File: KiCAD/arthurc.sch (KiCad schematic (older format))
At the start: 52 parts, among them IC1 ATMEGA328, P1 I/O, P10 CD2, P11 CD2, P12 CD1, P13 CD1, P4 CONN_6, P5 CONN_6, P6 9VBAT, P7 GPS, P8 FTDI, P9 ISP, SW1 SW_PUSH, U1 3V3, U2 74HC125, U3 5V0, X1 16MHz

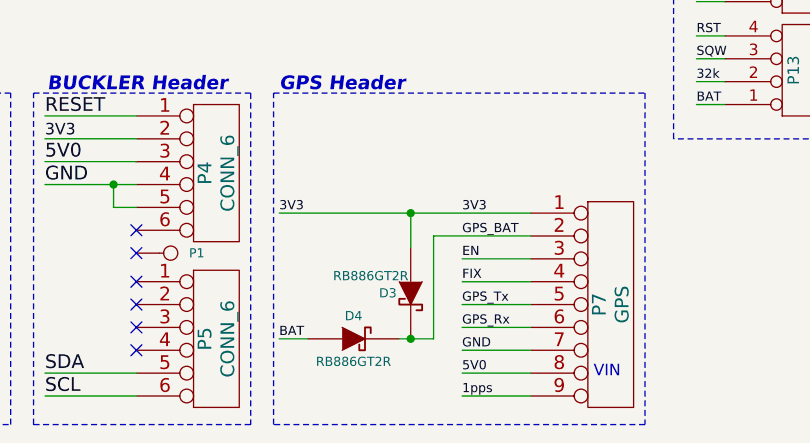
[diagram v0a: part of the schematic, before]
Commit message: Ultimate GPS header added to I2GPS
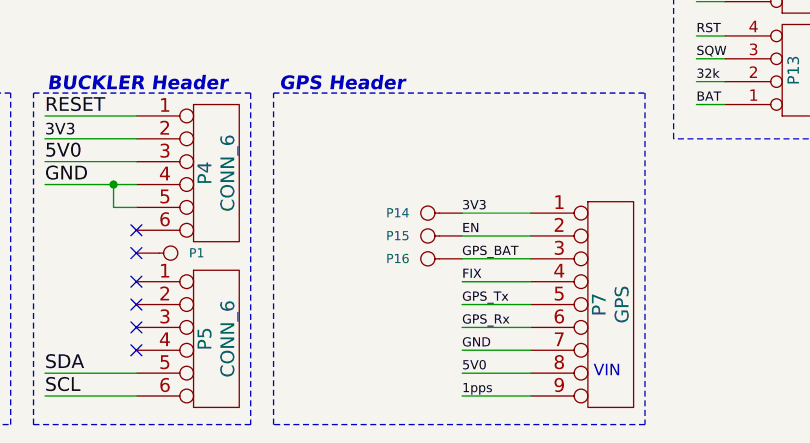
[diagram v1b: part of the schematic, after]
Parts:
- removed D3, D4: RB886GT2R, d_VMD2, symbol DIODESCH
- added P14, P15, P16: I/O, ArthurC Lib:I%2fO, symbol I/O
- B10, B11, B16, B17: footprint I/O_ADR -> ArthurC Lib:I%2fO_ADR
- B18, B19, B4, B5, B6, B8, P1: footprint I/O -> ArthurC Lib:I%2fO
- P7: footprint (none) -> ArthurC Lib:PIN_ARRAY-9X1
- X1: footprint (none) -> ArthurC Lib:Xtal_SMD3
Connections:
- wire segments 227 -> 223
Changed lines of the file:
@@
 MCP1700T-3302E/TT
-Wire Wire Line
-	5375 7375 5250 7375
 Wire Wire Line
 	3400 2750 4800 2750
@@
 Wire Wire Line
 	2450 4850 2450 5100
-Wire Wire Line
-	5775 7375 5925 7375
-Connection ~ 5825 7375
-$Comp
-L DIODESCH D4
-U 1 1 4F9A5A10
-P 5575 7375
-F 0 "D4" H 5575 7475 40  0000 C CNN
-F 1 "RB886GT2R" H 5575 7275 40  0000 C CNN
-F 2 "d_VMD2" H 5575 7375 40  0001 C CNN
-F 3 "" H 5575 7375 60  0001 C CNN
-	1    5575 7375
-	1    0    0    -1
-$EndComp
-$Comp
-L DIODESCH D3
-U 1 1 4F9A5A02
-P 5825 7175
-F 0 "D3" V 5825 7075 40  0000 C CNN
-F 1 "RB886GT2R" V 5750 7000 40  0000 C CNN
-F 2 "d_VMD2" V 5850 7000 40  0001 C CNN
-F 3 "" H 5825 7175 60  0001 C CNN
-	1    5825 7175
-	0    1    1    0
-$EndComp
 Text Label 1400 3275 0    50   ~ 0
 PB7
@@
 PB6
 $Comp
-L GND #PWR01
+L GND #PWR1
 U 1 1 4F5AFC62
 P 2450 5100
-F 0 "#PWR01" H 2450 5100 30  0001 C CNN
+F 0 "#PWR1" H 2450 5100 30  0001 C CNN
 F 1 "GND" H 2450 5030 30  0001 C CNN
 F 2 "" H 2450 5100 60  0001 C CNN
@@
 Text Notes 5250 6300 0    60   Italic 12
 GPS Header
-Text Label 5250 7375 0    40   ~ 0
-BAT
-Text Label 5250 6825 0    40   ~ 0
-3V3
 Text Label 10050 1450 0    50   ~ 0
 GND
@@
 IR SENSOR
 $Comp
-L GND #PWR02
+L GND #PWR3
 U 1 1 4EC6563E
 P 4100 2250
-F 0 "#PWR02" H 4100 2250 30  0001 C CNN
+F 0 "#PWR3" H 4100 2250 30  0001 C CNN
 F 1 "GND" H 4100 2180 30  0001 C CNN
 F 2 "" H 4100 2250 60  0001 C CNN
@@
 F 0 "B19" H 4280 1950 40  0000 L CNN
 F 1 "I/O" H 4200 2005 30  0001 C CNN
-F 2 "I/O" H 4200 1950 60  0001 C CNN
+F 2 "ArthurC Lib:I%2fO" H 4200 1950 60  0001 C CNN
 F 3 "" H 4200 1950 60  0001 C CNN
 	1    4200 1950
@@
 F 0 "B18" H 4180 1950 40  0000 L CNN
 F 1 "I/O" H 4100 2005 30  0001 C CNN
-F 2 "I/O" H 4100 1950 60  0001 C CNN
+F 2 "ArthurC Lib:I%2fO" H 4100 1950 60  0001 C CNN
 F 3 "" H 4100 1950 60  0001 C CNN
 	1    4100 1950
@@
 GND
 $Comp
-L GND #PWR03
+L GND #PWR4
 U 1 1 4E96D558
 P 4500 4600
-F 0 "#PWR03" H 4500 4600 30  0001 C CNN
+F 0 "#PWR4" H 4500 4600 30  0001 C CNN
 F 1 "GND" H 4500 4530 30  0001 C CNN
 F 2 "" H 4500 4600 60  0001 C CNN
@@
 F 0 "B17" H 4305 4150 40  0000 L CNN
 F 1 "I/O" H 4225 4205 30  0001 C CNN
-F 2 "I/O_ADR" H 4225 4150 60  0001 C CNN
+F 2 "ArthurC Lib:I%2fO_ADR" H 4225 4150 60  0001 C CNN
 F 3 "" H 4225 4150 60  0001 C CNN
 	1    4225 4150
@@
 F 0 "B16" H 4305 4050 40  0000 L CNN
 F 1 "I/O" H 4225 4105 30  0001 C CNN
-F 2 "I/O_ADR" H 4225 4050 60  0001 C CNN
+F 2 "ArthurC Lib:I%2fO_ADR" H 4225 4050 60  0001 C CNN
 F 3 "" H 4225 4050 60  0001 C CNN
 	1    4225 4050
@@
 F 0 "P1" H 4855 7000 40  0000 L CNN
 F 1 "I/O" H 4775 7055 30  0001 C CNN
-F 2 "I/O" H 4775 7000 60  0001 C CNN
+F 2 "ArthurC Lib:I%2fO" H 4775 7000 60  0001 C CNN
 F 3 "" H 4775 7000 60  0001 C CNN
 	1    4775 7000
@@
 GND
 $Comp
-L +3.3V #PWR04
+L +3.3V #PWR5
 U 1 1 4E1EF3E1
 P 7600 975
-F 0 "#PWR04" H 7600 935 30  0001 C CNN
+F 0 "#PWR5" H 7600 935 30  0001 C CNN
 F 1 "+3.3V" H 7600 1085 30  0000 C CNN
 F 2 "" H 7600 975 60  0001 C CNN
@@
 $EndComp
 $Comp
-L GND #PWR05
+L GND #PWR6
 U 1 1 4E1EC9C3
 P 9950 1525
-F 0 "#PWR05" H 9950 1525 30  0001 C CNN
+F 0 "#PWR6" H 9950 1525 30  0001 C CNN
 F 1 "GND" H 9950 1455 30  0001 C CNN
 F 2 "" H 9950 1525 60  0001 C CNN
@@
 LED2
 $Comp
-L GND #PWR06
+L GND #PWR2
 U 1 1 4DCFFB44
 P 3625 7550
-F 0 "#PWR06" H 3625 7550 30  0001 C CNN
+F 0 "#PWR2" H 3625 7550 30  0001 C CNN
 F 1 "GND" H 3625 7480 30  0001 C CNN
 F 2 "" H 3625 7550 60  0001 C CNN
@@
 F 0 "B11" H 3855 4050 40  0000 L CNN
 F 1 "I/O" H 3775 4105 30  0001 C CNN
-F 2 "I/O_ADR" H 3775 4050 60  0001 C CNN
+F 2 "ArthurC Lib:I%2fO_ADR" H 3775 4050 60  0001 C CNN
 F 3 "" H 3775 4050 60  0001 C CNN
 	1    3775 4050
@@
 F 0 "B10" H 3855 4150 40  0000 L CNN
 F 1 "I/O" H 3775 4205 30  0001 C CNN
-F 2 "I/O_ADR" H 3775 4150 60  0001 C CNN
+F 2 "ArthurC Lib:I%2fO_ADR" H 3775 4150 60  0001 C CNN
 F 3 "" H 3775 4150 60  0001 C CNN
 	1    3775 4150
@@
 F 0 "B8" H 3855 2950 40  0000 L CNN
 F 1 "I/O" H 3775 3005 30  0001 C CNN
-F 2 "I/O" H 3775 2950 60  0001 C CNN
+F 2 "ArthurC Lib:I%2fO" H 3775 2950 60  0001 C CNN
 F 3 "" H 3775 2950 60  0001 C CNN
 	1    3775 2950
@@
 F 0 "B6" H 3855 2350 40  0000 L CNN
 F 1 "I/O" H 3775 2405 30  0001 C CNN
-F 2 "I/O" H 3775 2350 60  0001 C CNN
+F 2 "ArthurC Lib:I%2fO" H 3775 2350 60  0001 C CNN
 F 3 "" H 3775 2350 60  0001 C CNN
 	1    3775 2350
@@
 F 0 "B5" H 3855 2450 40  0000 L CNN
 F 1 "I/O" H 3775 2505 30  0001 C CNN
-F 2 "I/O" H 3775 2450 60  0001 C CNN
+F 2 "ArthurC Lib:I%2fO" H 3775 2450 60  0001 C CNN
 F 3 "" H 3775 2450 60  0001 C CNN
 	1    3775 2450
@@
 F 0 "B4" H 4080 1950 40  0000 L CNN
 F 1 "I/O" H 4000 2005 30  0001 C CNN
-F 2 "I/O" H 4000 1950 60  0001 C CNN
+F 2 "ArthurC Lib:I%2fO" H 4000 1950 60  0001 C CNN
 F 3 "" H 4000 1950 60  0001 C CNN
 	1    4000 1950
@@
 GND
 $Comp
-L GND #PWR07
+L GND #PWR7
 U 1 1 4DCAC327
 P 9950 2475
-F 0 "#PWR07" H 9950 2475 30  0001 C CNN
+F 0 "#PWR7" H 9950 2475 30  0001 C CNN
 F 1 "GND" H 9950 2405 30  0001 C CNN
 F 2 "" H 9950 2475 60  0001 C CNN
@@
 F 0 "P7" V 6650 7225 60  0000 C CNN
 F 1 "GPS" V 6750 7225 60  0000 C CNN
-F 2 "" H 6700 7375 60  0000 C CNN
+F 2 "ArthurC Lib:PIN_ARRAY-9X1" H 6700 7375 60  0001 C CNN
 F 3 "" H 6700 7375 60  0000 C CNN
 	1    6700 7225
@@
 	6050 7125 6350 7125
 Wire Wire Line
-	5250 6825 6350 6825
-Wire Wire Line
-	5925 6925 6350 6925
-Wire Wire Line
 	6050 7025 6350 7025
+Text Label 6050 7025 0    40   ~ 0
+GPS_BAT
 Text Label 6050 6925 0    40   ~ 0
-GPS_BAT
-Text Label 6050 7025 0    40   ~ 0
 EN
 Text Label 6050 7125 0    40   ~ 0
@@
 Text Label 6050 7625 0    40   ~ 0
 1pps
-Wire Wire Line
-	5825 6975 5825 6825
-Wire Wire Line
-	5925 7375 5925 6925
-Connection ~ 5825 6825
 Text Label 6050 6825 0    40   ~ 0
 3V3
@@
 VIN
 $Comp
-L PWR_FLAG #FLG08
+L PWR_FLAG #FLG2
 U 1 1 53135BD8
 P 2450 750
-F 0 "#FLG08" H 2450 1020 30  0001 C CNN
+F 0 "#FLG2" H 2450 1020 30  0001 C CNN
 F 1 "PWR_FLAG" H 2450 980 30  0000 C CNN
 F 2 "" H 2450 750 60  0000 C CNN
@@
 $EndComp
 $Comp
-L PWR_FLAG #FLG09
+L PWR_FLAG #FLG1
 U 1 1 53135E05
 P 2350 5100
-F 0 "#FLG09" H 2350 5370 30  0001 C CNN
+F 0 "#FLG1" H 2350 5370 30  0001 C CNN
 F 1 "PWR_FLAG" H 2350 5330 30  0000 C CNN
 F 2 "" H 2350 5100 60  0000 C CNN
@@
 F 0 "X1" V 975 3300 60  0000 C CNN
 F 1 "16MHz" V 875 3375 60  0000 C CNN
-F 2 "" H 900 3050 60  0000 C CNN
+F 2 "ArthurC Lib:Xtal_SMD3" H 900 3050 60  0001 C CNN
 F 3 "" H 900 3050 60  0000 C CNN
 	1    900  3050
 	0    1    1    0
 $EndComp
+Wire Wire Line
+	6350 6825 6050 6825
+$Comp
+L I/O P14
+U 1 1 5339A614
+P 5900 6825
+F 0 "P14" H 5980 6825 40  0000 L CNN
+F 1 "I/O" H 5900 6880 30  0001 C CNN
+F 2 "ArthurC Lib:I%2fO" H 5900 6825 60  0001 C CNN
+F 3 "" H 5900 6825 60  0001 C CNN
+	1    5900 6825
+	-1   0    0    1
+$EndComp
+Wire Wire Line
+	6350 6925 6050 6925
+$Comp
+L I/O P15
+U 1 1 5339B720
+P 5900 6925
+F 0 "P15" H 5980 6925 40  0000 L CNN
+F 1 "I/O" H 5900 6980 30  0001 C CNN
+F 2 "ArthurC Lib:I%2fO" H 5900 6925 60  0001 C CNN
+F 3 "" H 5900 6925 60  0001 C CNN
+	1    5900 6925
+	-1   0    0    1
+$EndComp
+$Comp
+L I/O P16
+U 1 1 5339B72B
+P 5900 7025
+F 0 "P16" H 5980 7025 40  0000 L CNN
+F 1 "I/O" H 5900 7080 30  0001 C CNN
+F 2 "ArthurC Lib:I%2fO" H 5900 7025 60  0001 C CNN
+F 3 "" H 5900 7025 60  0001 C CNN
+	1    5900 7025
+	-1   0    0    1
+$EndComp
 $EndSCHEMATC

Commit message: work in progress, converting design to work on 3V3
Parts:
- removed C3: 2u2 Tant, c_0805, symbol C_POL
- removed C4, C8: 100n, c_0805, symbol C
- removed C6: 47u,10V, C_ELCO_SMD, symbol C_POL
- removed R3, R4, R6: 10k, r_0805, symbol R
- removed SD1: SD_CARD_MICRO, SD_Micro, symbol SD_CARD_MICRO
- removed U2: 74HC125, SO14E, symbol 74LS125
- removed U3: 5V0, SOT23-5, symbol MIC5219-5.0
- added P2: AREF, symbol CONN_2
- added SD1: SD_CARD_Micro, symbol SD_CARD_Micro
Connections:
- net labels removed: 5V0
- wire segments 223 -> 168
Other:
- note removed: "MIC5219-5.0BM5"

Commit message: ArthurC work in progress
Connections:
- net 3Vgps: now reaches P14.1, P7.1
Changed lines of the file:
@@
 Connection ~ 5000 800
 NoConn ~ 4625 6600
+Text Label 6075 6825 0    40   ~ 0
+3Vgps
 $EndSCHEMATC

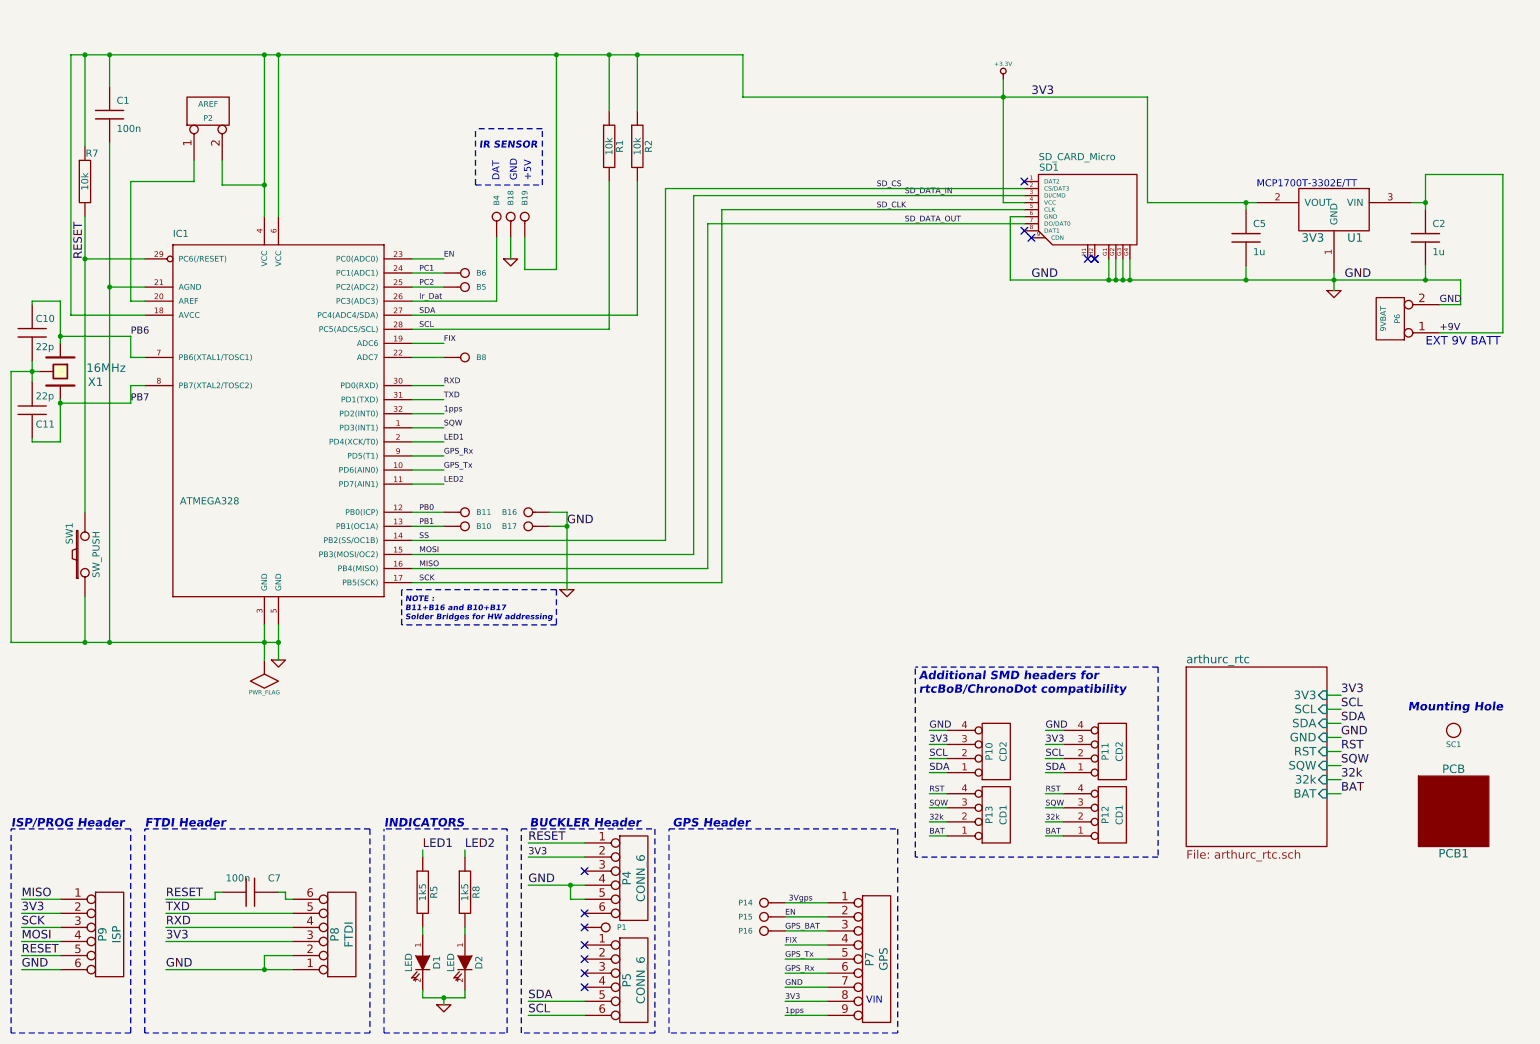
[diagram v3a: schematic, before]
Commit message: schematic needs final review before starting board layout
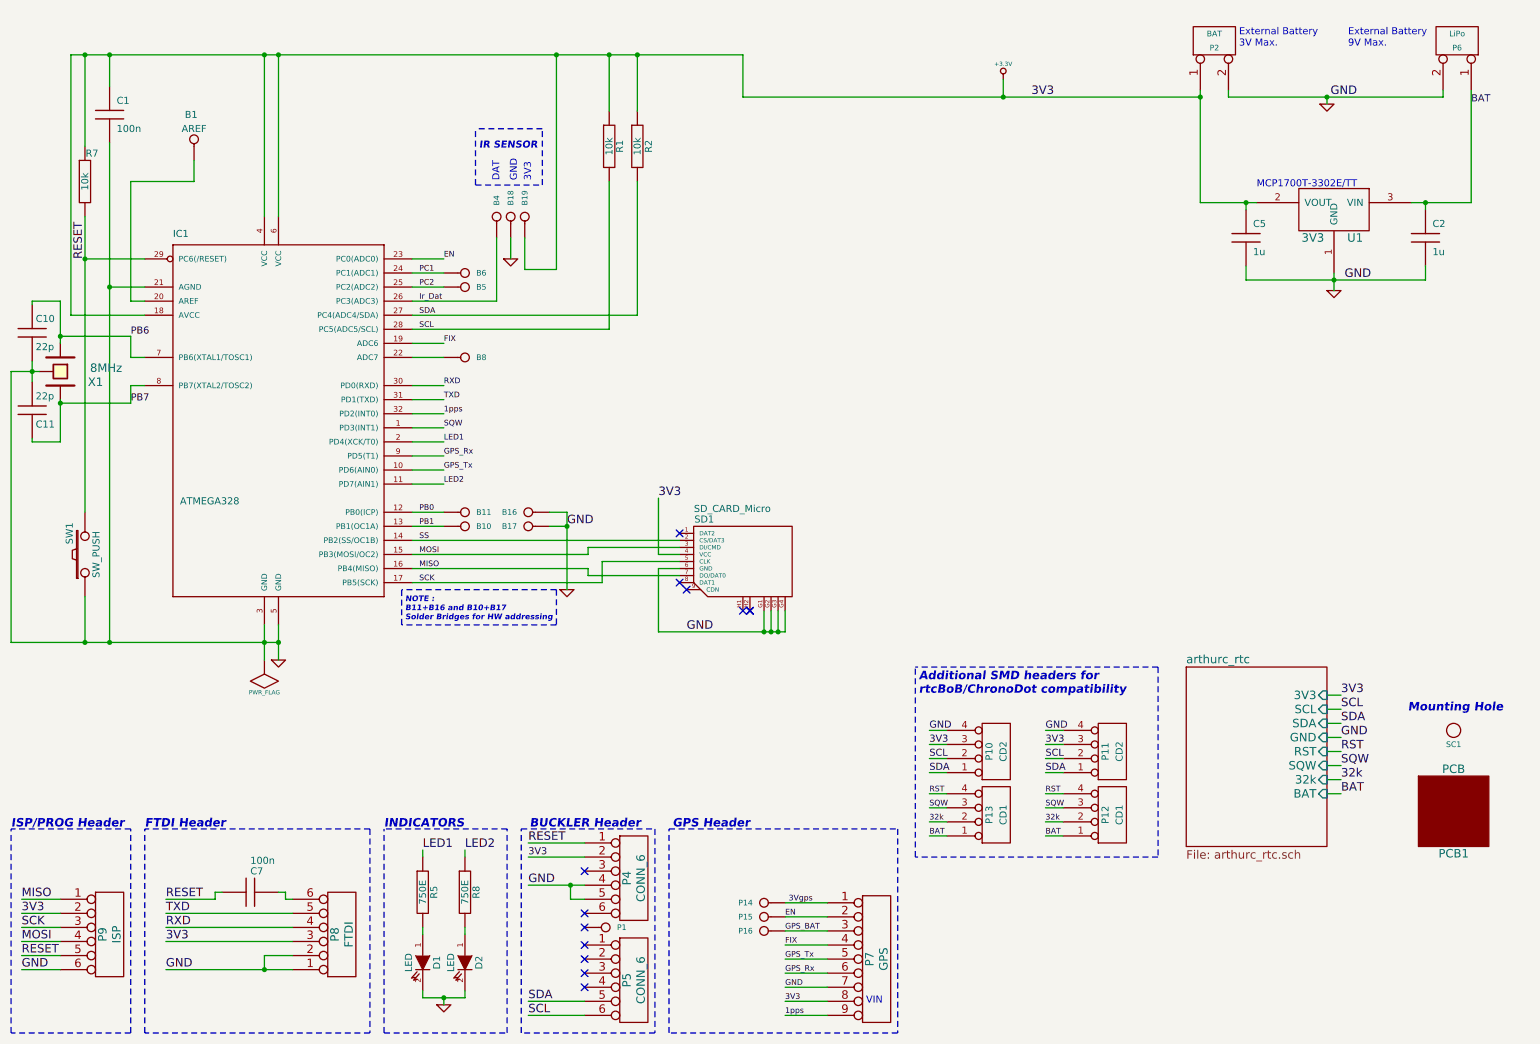
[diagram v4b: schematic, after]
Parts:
- added B1: AREF, symbol I/O
- P2: value AREF -> BAT
- P6: value 9VBAT -> LiPo
- R5, R8: value 1k5 -> 750E
- X1: value 16MHz -> 8MHz
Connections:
- net +9V is gone; now on net BAT: C2.1, P6.1 (P1), U1.3 (VIN)
- net +3.3V: now also P2.1 (P1); no longer P2.2 (PM)
- net GND: now also P2.2 (PM)
- net at IC1.20 (AREF): now also B1.1; no longer P2.1 (P1)
- net SD_CS renamed SS
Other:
- note added: "3V3"
- note added: "External Battery\n3V Max."
- note added: "External Battery\n9V Max."
- note removed: "+5V"
- note removed: "EXT 9V BATT"
- moved on the sheet: P6, SD1

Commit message: board layout work in progress
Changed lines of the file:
@@
 	4425 2325 4200 2325
 Wire Wire Line
-	550  3050 700  3050
-Wire Wire Line
-	700  3050 750  3050
+	550  3050 750  3050
 Connection ~ 900  3275
 Wire Wire Line
-	900  3250 900  3275
-Wire Wire Line
-	900  3275 900  3550
+	900  3250 900  3550
 Wire Wire Line
 	900  3550 700  3550
@@
 Connection ~ 1250 2450
 Wire Wire Line
-	1250 4975 1250 2450
-Wire Wire Line
-	1250 2450 1250 1425
+	1250 4975 1250 1425
 Connection ~ 2350 800
 Wire Wire Line
@@
 Connection ~ 5950 4900
 Wire Wire Line
-	2350 4850 2350 4975
-Wire Wire Line
-	2350 4975 2350 5100
+	2350 4850 2350 5100
 Wire Wire Line
 	2350 800  2350 1950
@@
 Connection ~ 1250 4975
 Wire Wire Line
-	9950 2350 9950 2400
-Wire Wire Line
-	9950 2400 9950 2475
+	9950 2350 9950 2475
 Wire Wire Line
 	4650 4300 4650 4350
@@
 	3775 7500 3775 7450
 Wire Wire Line
-	3475 7500 3625 7500
-Wire Wire Line
-	3625 7500 3775 7500
+	3475 7500 3775 7500
 Wire Wire Line
 	3475 7500 3475 7450
@@
 	2550 7100 1650 7100
 Wire Wire Line
-	5750 1100 7600 1100
-Wire Wire Line
-	7600 1100 9000 1100
-Wire Wire Line
-	9000 1100 9000 1100
-Wire Wire Line
-	9000 1100 9000 1850
-Wire Wire Line
-	9000 1850 9325 1850
-Wire Wire Line
-	9325 1850 9400 1850
-Wire Wire Line
-	10500 1850 10600 1850
-Wire Wire Line
-	10600 1850 10925 1850
-Wire Wire Line
-	975  800  1075 800
-Wire Wire Line
-	1075 800  1250 800
-Wire Wire Line
-	1250 800  2350 800
-Wire Wire Line
-	2350 800  2450 800
-Wire Wire Line
-	2450 800  4425 800
-Wire Wire Line
-	4425 800  4800 800
-Wire Wire Line
-	4800 800  5000 800
-Wire Wire Line
-	5000 800  5750 800
-Wire Wire Line
-	1650 7300 2350 7300
-Wire Wire Line
-	2350 7300 2550 7300
+	5750 1100 9000 1100
+Wire Wire Line
+	9000 1050 9000 1850
+Wire Wire Line
+	9000 1850 9400 1850
+Wire Wire Line
+	10500 1850 10925 1850
+Wire Wire Line
+	975  800  5750 800
+Wire Wire Line
+	1650 7300 2550 7300
 Wire Wire Line
 	2550 6900 1650 6900
@@
 	4625 6400 4225 6400
 Wire Wire Line
-	4225 6700 4525 6700
-Wire Wire Line
-	4525 6700 4625 6700
+	4225 6700 4625 6700
 Wire Notes Line
 	3100 6300 1500 6300
@@
 	4625 7625 4225 7625
 Wire Wire Line
-	1075 1950 1075 2250
-Wire Wire Line
-	1075 2250 1075 4050
+	1075 1950 1075 4050
 Connection ~ 1075 2250
 Wire Wire Line
@@
 	4375 4050 4500 4050
 Wire Wire Line
-	4500 4050 4500 4150
-Wire Wire Line
-	4500 4150 4500 4600
+	4500 4050 4500 4600
 Wire Notes Line
 	4425 4600 3325 4600
@@
 	5150 4450 5150 4900
 Wire Wire Line
-	5150 4900 5900 4900
-Wire Wire Line
-	5900 4900 5950 4900
-Wire Wire Line
-	5950 4900 6000 4900
-Wire Wire Line
-	6000 4900 6050 4900
-Wire Wire Line
-	9325 2400 9950 2400
-Wire Wire Line
-	9950 2400 10600 2400
+	5150 4900 6050 4900
+Wire Wire Line
+	9325 2400 10600 2400
 Wire Wire Line
 	6050 4900 6050 4750
@@
 	5950 4900 5950 4750
 Wire Wire Line
-	700  2975 700  3050
-Wire Wire Line
-	700  3050 700  3125
+	700  2975 700  3125
 Wire Wire Line
 	700  2575 700  2550
@@
 	700  2550 900  2550
 Wire Wire Line
-	900  2550 900  2800
-Wire Wire Line
-	900  2800 900  2850
+	900  2550 900  2850
 Connection ~ 900  2800
 Wire Wire Line
 	550  3050 550  4975
 Wire Wire Line
-	550  4975 1075 4975
-Wire Wire Line
-	1075 4975 1250 4975
-Wire Wire Line
-	1250 4975 2350 4975
-Wire Wire Line
-	2350 4975 2450 4975
+	550  4975 2450 4975
 Wire Wire Line
 	4000 2100 4000 2550
@@
 	9900 5850 10000 5850
 Wire Wire Line
-	2450 4850 2450 4975
-Wire Wire Line
-	2450 4975 2450 5100
+	2450 4850 2450 5100
 Text Label 1400 3275 0    50   ~ 0
 PB7
@@
 	0    -1   -1   0
 $EndComp
-Wire Wire Line
-	9000 1100 9000 1050
 Connection ~ 9000 1100
 Wire Wire Line
@@
 3V3
 Wire Wire Line
-	9200 1100 9900 1100
-Wire Wire Line
-	9900 1100 10725 1100
+	9200 1100 10725 1100
 Wire Wire Line
 	10725 1100 10725 1050
